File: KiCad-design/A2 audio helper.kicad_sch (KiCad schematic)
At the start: 35 parts, among them J1 PIN HEADER 1x2, J10 PIN HEADER 1x2, J11 PIN HEADER 1x3, J12 PIN HEADER 1x3, J13 PIN HEADER 1x3, J14 PIN HEADER 2x6, J2 PIN HEADER 1x2, J3 PIN HEADER 1x2, J4 SJ1-3515N, J5 PIN HEADER 1x3, J6 PIN HEADER 1x3, J7 SJ1-3515N, J8 PIN HEADER 1x5, J9 PIN HEADER 1x2, K1 SR11-5V-200-2C, SW2 SW_DPDT_x2, U1 pam8403

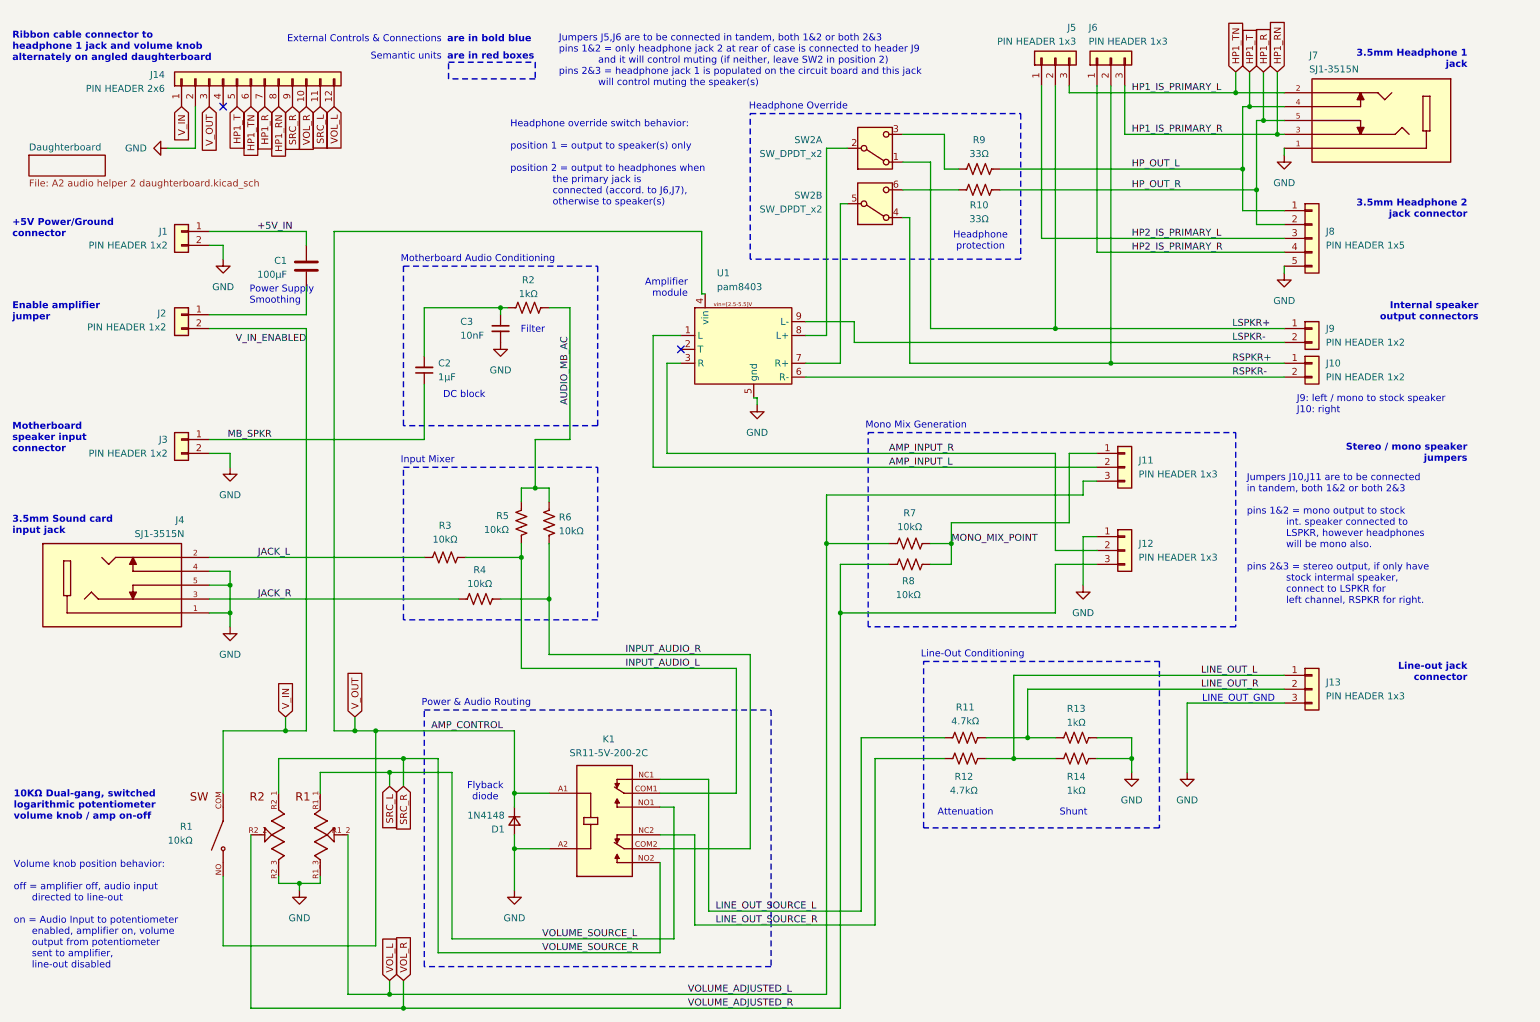
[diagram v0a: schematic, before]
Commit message: fixed dual headphones
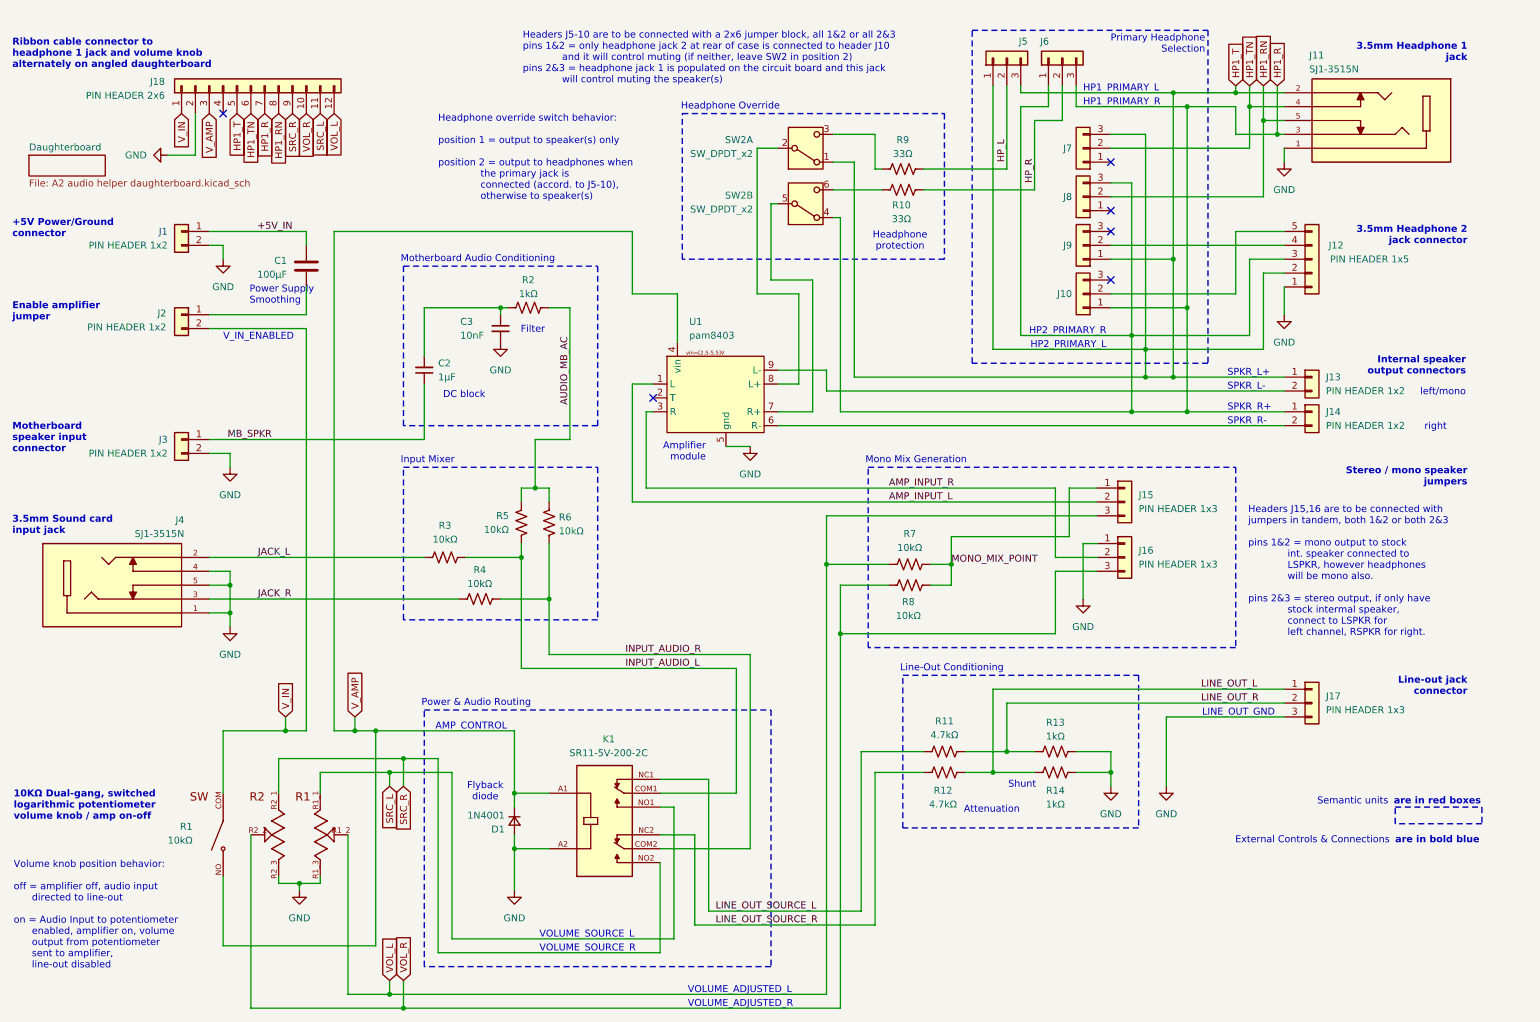
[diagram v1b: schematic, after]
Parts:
- added J10, J7, J8, J9: Conn_01x03, Connector_PinHeader_2.54mm:PinHeader_1x03_P2.54mm_Vertical, symbol Connector_Generic:Conn_01x03
- D1: value 1N4148 -> 1N4001; footprint Diode_THT:D_DO-35_SOD27_P7.62mm_Horizontal -> Diode_THT:D_DO-35_SOD27_P2.54mm_Vertical_AnodeUp
- renumbered J7 to J11, J8 to J12, J9 to J13, J10 to J14, J11 to J15, J12 to J16, J13 to J17, J14 to J18
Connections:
- net GND: now also J12.1 (Pin_1); no longer J12.5 (Pin_5)
- net HP1_R: now also J11.3, J12.3 (Pin_3), J14.1 (Pin_1), J6.1 (Pin_1), J6.3 (Pin_3), SW2.4 (A), J10.1 (Pin_1), J8.3 (Pin_3); no longer J11.5, J12.2 (Pin_2), R10.2
- net HP1_RN: now also J11.5, J8.2 (Pin_2); no longer J11.3, J6.3 (Pin_3)
- net HP1_T: now also J11.2, J12.2 (Pin_2), J13.1 (Pin_1), J5.1 (Pin_1), J5.3 (Pin_3), SW2.1 (A), J7.3 (Pin_3), J9.1 (Pin_1); no longer J11.4, J12.1 (Pin_1), R9.2
- net HP1_TN: now also J11.4, J7.2 (Pin_2); no longer J11.2, J5.3 (Pin_3)
- removed net HP2_IS_PRIMARY_L: J12.3 (Pin_3), J5.1 (Pin_1)
- net HP2_IS_PRIMARY_R: no longer names the net of J12.4 (Pin_4)
- net HP2_IS_PRIMARY_R: now also J9.2 (Pin_2); no longer J6.1 (Pin_1)
- removed net LSPKR+: J13.1 (Pin_1), J5.2 (Pin_2), SW2.1 (A)
- net LSPKR-: no longer names the net of J13.2 (Pin_2), U1.9 (L-)
- removed net RSPKR+: J14.1 (Pin_1), J6.2 (Pin_2), SW2.4 (A)
- net RSPKR-: no longer names the net of J14.2 (Pin_2), U1.6 (R-)
- net V_OUT renamed V_AMP
- new net: J10.2 (Pin_2), J12.5 (Pin_5)
- new net HP_L: J5.2 (Pin_2), R9.2
- new net HP_R: J6.2 (Pin_2), R10.2
- no-connect marks 2 -> 6
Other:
- sheet Daughterboard: file A2 audio helper 2 daughterboard.kicad_sch -> A2 audio helper daughterboard.kicad_sch
- note added: "AMP_CONTROL"
- note added: "HP1_PRIMARY_L"
- note added: "HP1_PRIMARY_R"
- note added: "HP2_PRIMARY_L"
- note added: "HP2_PRIMARY_R"
- note added: "Headers J15,16 are to be connected with jumpers in tandem, both 1&2 or both 2&3 pins 1&2 = mono output to stock int. speaker connected to LSPKR, however headphones will be mono also. pins 2&3 = stereo output, if only have stock intermal speaker, connect to LSPKR for left channel, RSPKR for right."
- note added: "Headers J5-10 are to be connected with a 2x6 jumper block, all 1&2 or all 2&3 pins 1&2 = only headphone jack 2 at rear of case is connected to header J10 and it will control muting (if neither, leave SW2 in position 2) pins 2&3 = headphone jack 1 is populated on the circuit board and this jack will control muting the speaker(s)"
- note added: "Headphone override switch behavior: position 1 = output to speaker(s) only position 2 = output to headphones when the primary jack is connected (accord. to J5-10), otherwise to speaker(s)"
- note added: "Primary Headphone Selection"
- note added: "SPKR_L+"
- note added: "SPKR_L-"
- note added: "SPKR_R+"
- note added: "SPKR_R-"
- note added: "VOLUME_ADJUSTED_L"
- note added: "VOLUME_ADJUSTED_R"
- note added: "VOLUME_SOURCE_L"
- note added: "VOLUME_SOURCE_R"
- note added: "V_IN_ENABLED"
- note added: "left/mono"
- note added: "right"
- note removed: "Headphone override switch behavior: position 1 = output to speaker(s) only position 2 = output to headphones when the primary jack is connected (accord. to J6,J7), otherwise to speaker(s)"
- note removed: "J9: left / mono to stock speaker J10: right"
- note removed: "Jumpers J10,J11 are to be connected in tandem, both 1&2 or both 2&3 pins 1&2 = mono output to stock int. speaker connected to LSPKR, however headphones will be mono also. pins 2&3 = stereo output, if only have stock intermal speaker, connect to LSPKR for left channel, RSPKR for right."
- note removed: "Jumpers J5,J6 are to be connected in tandem, both 1&2 or both 2&3 pins 1&2 = only headphone jack 2 at rear of case is connected to header J9 and it will control muting (if neither, leave SW2 in position 2) pins 2&3 = headphone jack 1 is populated on the circuit board and this jack will control muting the speaker(s)"
- moved on the sheet: J12, J13, J14, J15, J16, J17, J18, J5, J6, R10, R11, R12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

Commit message: improved fix for dual headphones
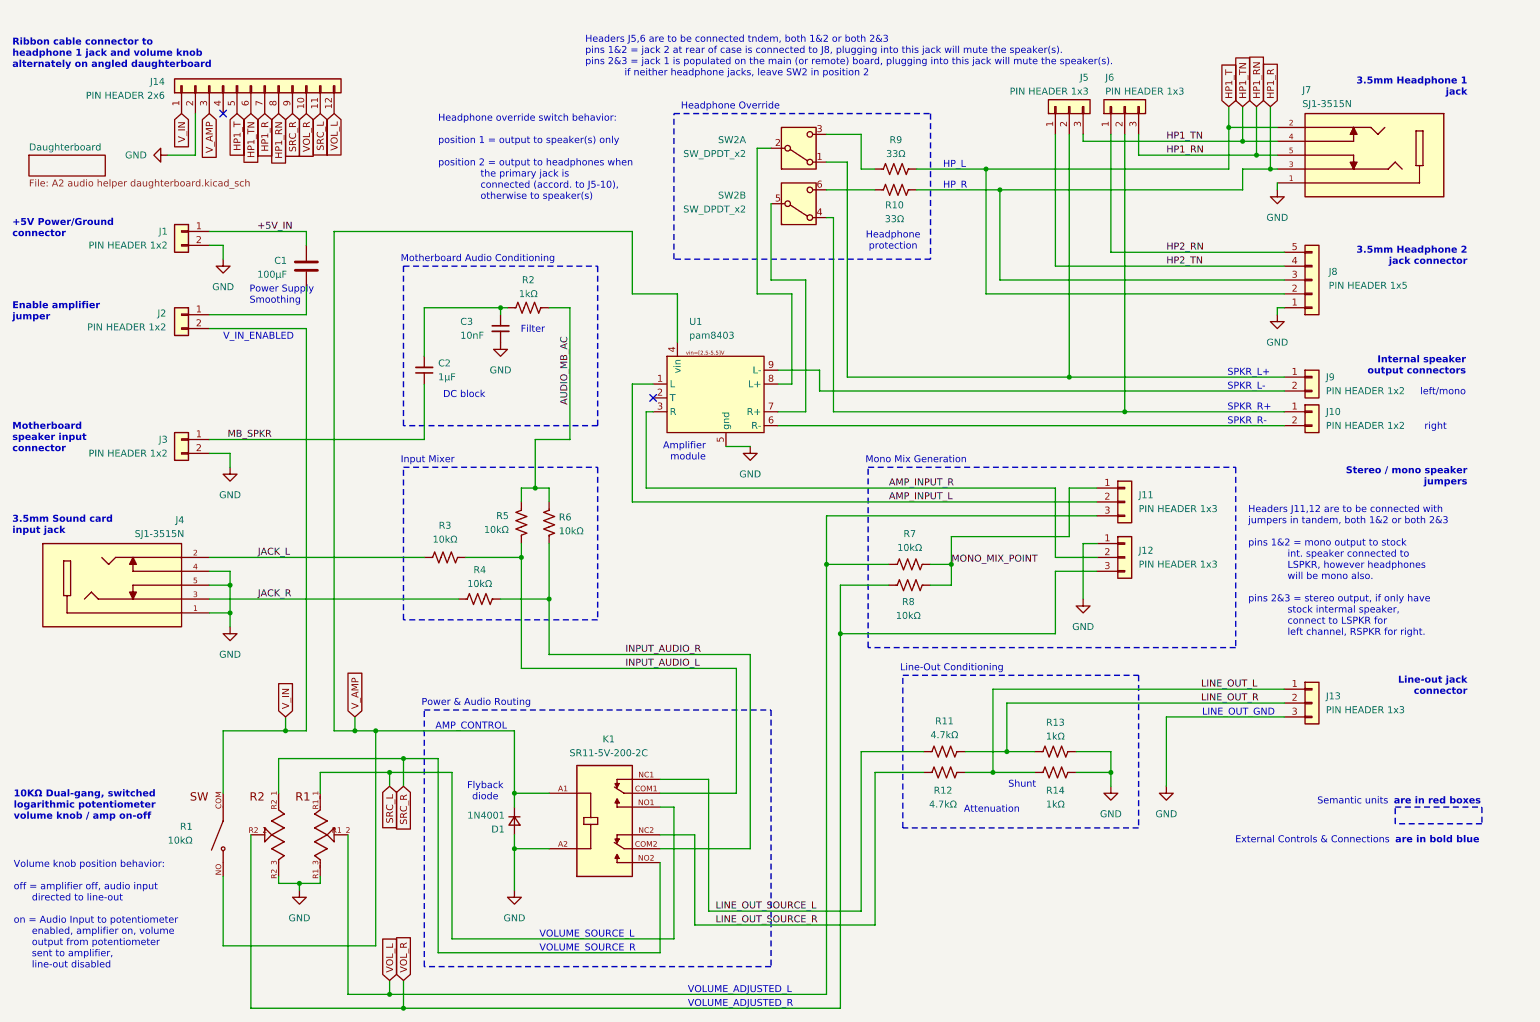
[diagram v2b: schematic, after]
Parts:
- removed J10, J7, J8, J9: Conn_01x03, Connector_PinHeader_2.54mm:PinHeader_1x03_P2.54mm_Vertical, symbol Connector_Generic:Conn_01x03
- D1: footprint Diode_THT:D_DO-35_SOD27_P2.54mm_Vertical_AnodeUp -> Diode_THT:D_DO-35_SOD27_P7.62mm_Horizontal
- J5, J6: footprint Connector_PinHeader_2.54mm:PinHeader_1x03_P2.54mm_Vertical -> (none)
- renumbered J14 to J10, J15 to J11, J16 to J12, J17 to J13, J18 to J14, J11 to J7, J12 to J8, J13 to J9
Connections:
- net HP1_R: now also R10.2; no longer J10.1 (Pin_1), J6.1 (Pin_1), J6.3 (Pin_3), SW2.4 (A)
- net HP1_RN: now also J6.3 (Pin_3)
- net HP1_T: now also R9.2; no longer J5.1 (Pin_1), J5.3 (Pin_3), J9.1 (Pin_1), SW2.1 (A)
- net HP1_TN: now also J5.3 (Pin_3)
- net HP2_TN: now reaches J8.4 (Pin_4)
- net HP2_TN: now also J5.1 (Pin_1)
- net HP2_RN: now reaches J8.5 (Pin_5)
- net HP2_RN: now also J6.1 (Pin_1)
- net HP_L: no longer names the net of J5.2 (Pin_2)
- net HP_L: now also J9.1 (Pin_1), SW2.1 (A); no longer R9.2
- net HP_R: no longer names the net of J6.2 (Pin_2)
- net HP_R: now also J10.1 (Pin_1), SW2.4 (A); no longer R10.2
- no-connect marks 6 -> 2
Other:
- note added: "HP_L"
- note added: "HP_R"
- note added: "Headers J11,12 are to be connected with jumpers in tandem, both 1&2 or both 2&3 pins 1&2 = mono output to stock int. speaker connected to LSPKR, however headphones will be mono also. pins 2&3 = stereo output, if only have stock intermal speaker, connect to LSPKR for left channel, RSPKR for right."
- note added: "Headers J5,6 are to be connected tndem, both 1&2 or both 2&3 pins 1&2 = jack 2 at rear of case is connected to J8, plugging into this jack will mute the speaker(s). pins 2&3 = jack 1 is populated on the main (or remote) board, plugging into this jack will mute the speaker(s). if neither headphone jacks, leave SW2 in position 2"
- note removed: "HP1_PRIMARY_L"
- note removed: "HP1_PRIMARY_R"
- note removed: "HP2_PRIMARY_L"
- note removed: "HP2_PRIMARY_R"
- note removed: "Headers J15,16 are to be connected with jumpers in tandem, both 1&2 or both 2&3 pins 1&2 = mono output to stock int. speaker connected to LSPKR, however headphones will be mono also. pins 2&3 = stereo output, if only have stock intermal speaker, connect to LSPKR for left channel, RSPKR for right."
- note removed: "Headers J5-10 are to be connected with a 2x6 jumper block, all 1&2 or all 2&3 pins 1&2 = only headphone jack 2 at rear of case is connected to header J10 and it will control muting (if neither, leave SW2 in position 2) pins 2&3 = headphone jack 1 is populated on the circuit board and this jack will control muting the speaker(s)"
- note removed: "Primary Headphone Selection"
- moved on the sheet: J7, J8, R10, R9, SW2A, SW2B
